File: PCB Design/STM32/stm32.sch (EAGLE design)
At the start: 58 parts, among them IC1 NCP1117ST50T3G, Q1 8MHz, T1 SFH303, T2 SFH303, T3 SFH303, T4 SFH303, U1 STM32F103RET6, U2 MCP1700T-3302E/TT, U3 MCP1700T-3302E/TT, U4 MPU-6050, U5 TB6612FNG

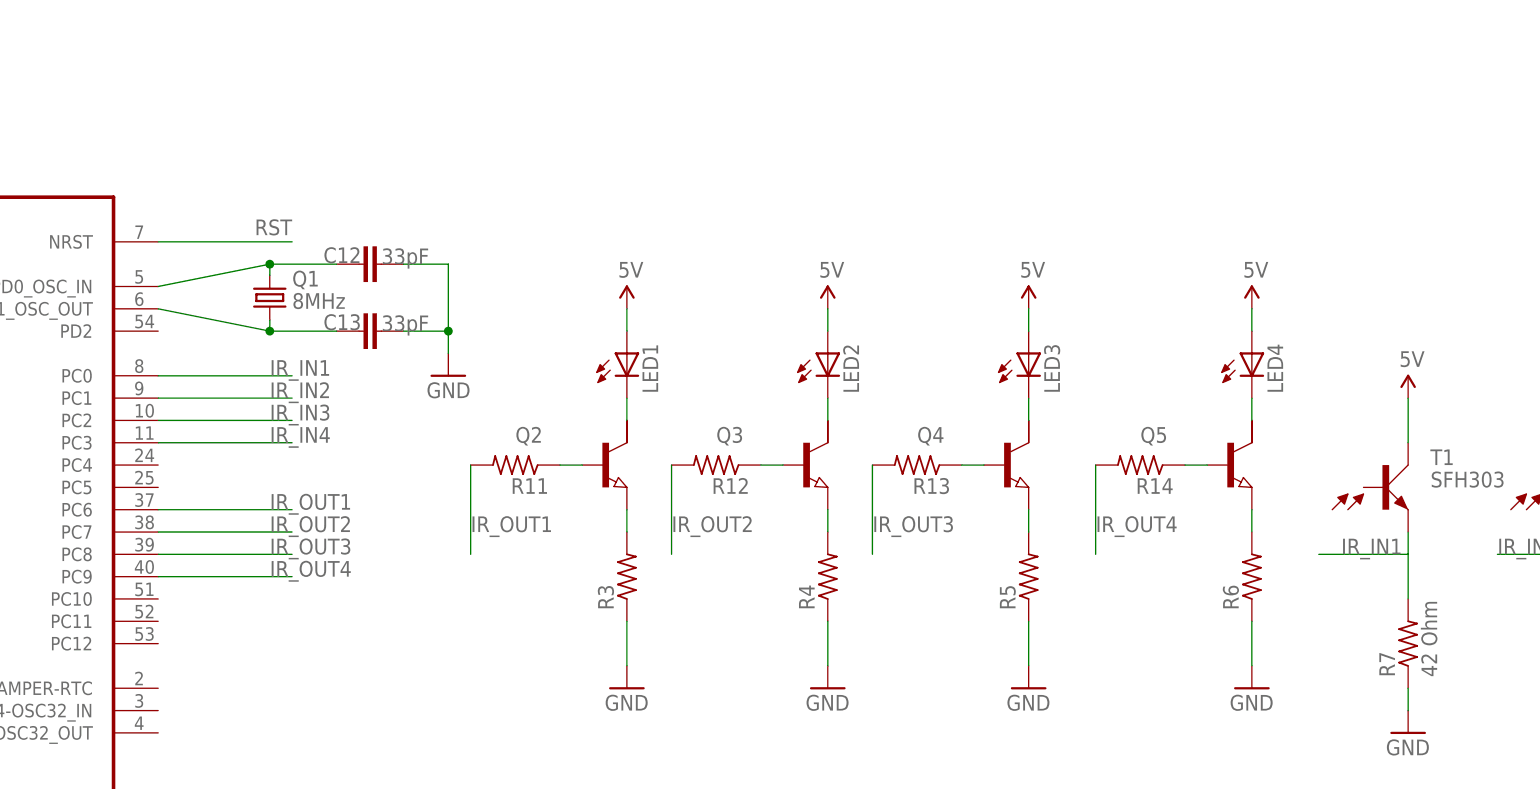
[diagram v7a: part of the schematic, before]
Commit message: added indicating leds
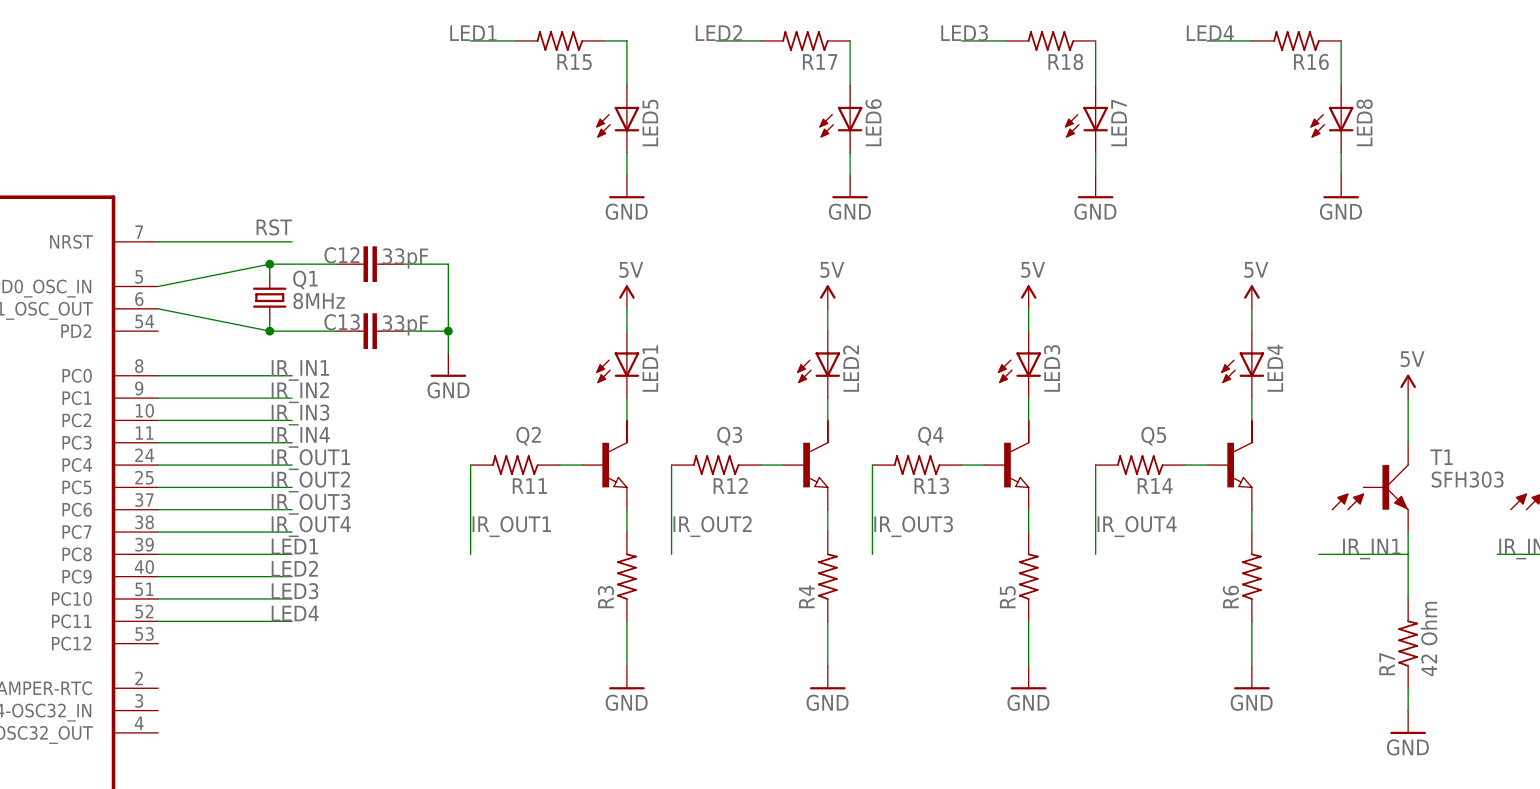
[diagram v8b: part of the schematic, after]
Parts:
- added LED5, LED6, LED7, LED8: (no value), eagle-ltspice:LED_ESML0603
- added R15, R16, R17, R18: (no value), resistor:R-US_R0603
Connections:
- new net LED1: R15.2, U1.PC8
- new net LED2: R17.2, U1.PC9
- new net LED3: R18.2
- new net LED4: R16.2
- new net N$26: LED5.A, R15.1
- new net N$27: LED6.A, R17.1
- new net N$28: LED7.A, R18.1
- new net N$29: LED8.A, R16.1
- net GND: now also LED5.C, LED6.C, LED7.C, LED8.C
- net IR_OUT1: no longer U1.PC6
- net IR_OUT2: no longer U1.PC7
- net IR_OUT3: now also U1.PC6; no longer U1.PC8
- net IR_OUT4: now also U1.PC7; no longer U1.PC9
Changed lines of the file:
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@@
 <?xml version="1.0" encoding="utf-8"?>
 <!DOCTYPE eagle SYSTEM "eagle.dtd">
-<eagle version="7.2.0">
+<eagle version="7.1.0">
 <drawing>
 <settings>
@@
 <part name="R13" library="resistor" deviceset="R-US_" device="R0603"/>
 <part name="R14" library="resistor" deviceset="R-US_" device="R0603"/>
+<part name="LED5" library="eagle-ltspice" deviceset="LED_E" device="SML0603"/>
+<part name="LED6" library="eagle-ltspice" deviceset="LED_E" device="SML0603"/>
+<part name="LED7" library="eagle-ltspice" deviceset="LED_E" device="SML0603"/>
+<part name="LED8" library="eagle-ltspice" deviceset="LED_E" device="SML0603"/>
+<part name="R15" library="resistor" deviceset="R-US_" device="R0603"/>
+<part name="R16" library="resistor" deviceset="R-US_" device="R0603"/>
+<part name="R17" library="resistor" deviceset="R-US_" device="R0603"/>
+<part name="R18" library="resistor" deviceset="R-US_" device="R0603"/>
+<part name="GND6" library="supply1" deviceset="GND" device=""/>
+<part name="GND29" library="supply1" deviceset="GND" device=""/>
+<part name="GND36" library="supply1" deviceset="GND" device=""/>
+<part name="GND37" library="supply1" deviceset="GND" device=""/>
 </parts>
 <sheets>
@@
 <instance part="R13" gate="G$1" x="309.88" y="236.22" rot="R180"/>
 <instance part="R14" gate="G$1" x="335.28" y="236.22" rot="R180"/>
+<instance part="LED5" gate="G$1" x="276.86" y="276.86"/>
+<instance part="LED6" gate="G$1" x="302.26" y="276.86"/>
+<instance part="LED7" gate="G$1" x="330.2" y="276.86"/>
+<instance part="LED8" gate="G$1" x="358.14" y="276.86"/>
+<instance part="R15" gate="G$1" x="269.24" y="284.48" rot="R180"/>
+<instance part="R16" gate="G$1" x="353.06" y="284.48" rot="R180"/>
+<instance part="R17" gate="G$1" x="297.18" y="284.48" rot="R180"/>
+<instance part="R18" gate="G$1" x="325.12" y="284.48" rot="R180"/>
+<instance part="GND6" gate="1" x="276.86" y="266.7"/>
+<instance part="GND29" gate="1" x="302.26" y="266.7"/>
+<instance part="GND36" gate="1" x="330.2" y="266.7"/>
+<instance part="GND37" gate="1" x="358.14" y="266.7"/>
 </instances>
 <busses>
@@
 <wire x1="347.98" y1="218.44" x2="347.98" y2="213.36" width="0.1524" layer="91"/>
 </segment>
+<segment>
+<pinref part="LED5" gate="G$1" pin="C"/>
+<pinref part="GND6" gate="1" pin="GND"/>
+<wire x1="276.86" y1="271.78" x2="276.86" y2="269.24" width="0.1524" layer="91"/>
+</segment>
+<segment>
+<pinref part="LED6" gate="G$1" pin="C"/>
+<pinref part="GND29" gate="1" pin="GND"/>
+<wire x1="302.26" y1="271.78" x2="302.26" y2="269.24" width="0.1524" layer="91"/>
+</segment>
+<segment>
+<pinref part="LED7" gate="G$1" pin="C"/>
+<pinref part="GND36" gate="1" pin="GND"/>
+<wire x1="330.2" y1="271.78" x2="330.2" y2="269.24" width="0.1524" layer="91"/>
+</segment>
+<segment>
+<pinref part="LED8" gate="G$1" pin="C"/>
+<pinref part="GND37" gate="1" pin="GND"/>
+<wire x1="358.14" y1="271.78" x2="358.14" y2="269.24" width="0.1524" layer="91"/>
+</segment>
 </net>
 <net name="VCC" class="0">
@@
 <net name="IR_OUT2" class="0">
 <segment>
-<wire x1="223.52" y1="228.6" x2="238.76" y2="228.6" width="0.1524" layer="91"/>
-<label x="236.22" y="228.6" size="1.778" layer="95"/>
-<pinref part="U1" gate="A" pin="PC7"/>
-</segment>
-<segment>
 <pinref part="R12" gate="G$1" pin="2"/>
 <wire x1="281.94" y1="236.22" x2="281.94" y2="226.06" width="0.1524" layer="91"/>
 <label x="281.94" y="228.6" size="1.778" layer="95"/>
 </segment>
+<segment>
+<wire x1="223.52" y1="233.68" x2="238.76" y2="233.68" width="0.1524" layer="91"/>
+<label x="236.22" y="233.68" size="1.778" layer="95"/>
+</segment>
 </net>
 <net name="IR_OUT1" class="0">
+<segment>
+<pinref part="R11" gate="G$1" pin="2"/>
+<wire x1="259.08" y1="236.22" x2="259.08" y2="226.06" width="0.1524" layer="91"/>
+<label x="259.08" y="228.6" size="1.778" layer="95"/>
+</segment>
+<segment>
+<wire x1="223.52" y1="236.22" x2="238.76" y2="236.22" width="0.1524" layer="91"/>
+<label x="236.22" y="236.22" size="1.778" layer="95"/>
+</segment>
+</net>
+<net name="IR_OUT3" class="0">
+<segment>
+<pinref part="R13" gate="G$1" pin="2"/>
+<wire x1="304.8" y1="236.22" x2="304.8" y2="226.06" width="0.1524" layer="91"/>
+<label x="304.8" y="228.6" size="1.778" layer="95"/>
+</segment>
 <segment>
 <wire x1="223.52" y1="231.14" x2="238.76" y2="231.14" width="0.1524" layer="91"/>
 <label x="236.22" y="231.14" size="1.778" layer="95"/>
 <pinref part="U1" gate="A" pin="PC6"/>
-</segment>
-<segment>
-<pinref part="R11" gate="G$1" pin="2"/>
-<wire x1="259.08" y1="236.22" x2="259.08" y2="226.06" width="0.1524" layer="91"/>
-<label x="259.08" y="228.6" size="1.778" layer="95"/>
-</segment>
-</net>
-<net name="IR_OUT3" class="0">
-<segment>
-<wire x1="223.52" y1="226.06" x2="238.76" y2="226.06" width="0.1524" layer="91"/>
-<label x="236.22" y="226.06" size="1.778" layer="95"/>
-<pinref part="U1" gate="A" pin="PC8"/>
-</segment>
-<segment>
-<pinref part="R13" gate="G$1" pin="2"/>
-<wire x1="304.8" y1="236.22" x2="304.8" y2="226.06" width="0.1524" layer="91"/>
-<label x="304.8" y="228.6" size="1.778" layer="95"/>
 </segment>
 </net>
@@
 <net name="IR_OUT4" class="0">
 <segment>
-<wire x1="223.52" y1="223.52" x2="238.76" y2="223.52" width="0.1524" layer="91"/>
-<label x="236.22" y="223.52" size="1.778" layer="95"/>
-<pinref part="U1" gate="A" pin="PC9"/>
-</segment>
-<segment>
 <pinref part="R14" gate="G$1" pin="2"/>
 <wire x1="330.2" y1="236.22" x2="330.2" y2="226.06" width="0.1524" layer="91"/>
 <label x="330.2" y="228.6" size="1.778" layer="95"/>
+</segment>
+<segment>
+<wire x1="223.52" y1="228.6" x2="238.76" y2="228.6" width="0.1524" layer="91"/>
+<label x="236.22" y="228.6" size="1.778" layer="95"/>
+<pinref part="U1" gate="A" pin="PC7"/>
 </segment>
 </net>
@@
 </segment>
 </net>
+<net name="N$26" class="0">
+<segment>
+<pinref part="R15" gate="G$1" pin="1"/>
+<pinref part="LED5" gate="G$1" pin="A"/>
+<wire x1="274.32" y1="284.48" x2="276.86" y2="284.48" width="0.1524" layer="91"/>
+<wire x1="276.86" y1="284.48" x2="276.86" y2="279.4" width="0.1524" layer="91"/>
+</segment>
+</net>
+<net name="N$27" class="0">
+<segment>
+<pinref part="R17" gate="G$1" pin="1"/>
+<pinref part="LED6" gate="G$1" pin="A"/>
+<wire x1="302.26" y1="284.48" x2="302.26" y2="279.4" width="0.1524" layer="91"/>
+</segment>
+</net>
+<net name="N$29" class="0">
+<segment>
+<pinref part="R16" gate="G$1" pin="1"/>
+<pinref part="LED8" gate="G$1" pin="A"/>
+<wire x1="358.14" y1="284.48" x2="358.14" y2="279.4" width="0.1524" layer="91"/>
+</segment>
+</net>
+<net name="N$28" class="0">
+<segment>
+<pinref part="R18" gate="G$1" pin="1"/>
+<pinref part="LED7" gate="G$1" pin="A"/>
+<wire x1="330.2" y1="284.48" x2="330.2" y2="279.4" width="0.1524" layer="91"/>
+</segment>
+</net>
+<net name="LED1" class="0">
+<segment>
+<wire x1="223.52" y1="226.06" x2="238.76" y2="226.06" width="0.1524" layer="91"/>
+<label x="236.22" y="226.06" size="1.778" layer="95"/>
+<pinref part="U1" gate="A" pin="PC8"/>
+</segment>
+<segment>
+<pinref part="R15" gate="G$1" pin="2"/>
+<wire x1="264.16" y1="284.48" x2="259.08" y2="284.48" width="0.1524" layer="91"/>
+<label x="256.54" y="284.48" size="1.778" layer="95"/>
+</segment>
+</net>
+<net name="LED2" class="0">
+<segment>
+<wire x1="223.52" y1="223.52" x2="238.76" y2="223.52" width="0.1524" layer="91"/>
+<label x="236.22" y="223.52" size="1.778" layer="95"/>
+<pinref part="U1" gate="A" pin="PC9"/>
+</segment>
+<segment>
+<pinref part="R17" gate="G$1" pin="2"/>
+<wire x1="292.1" y1="284.48" x2="287.02" y2="284.48" width="0.1524" layer="91"/>
+<label x="284.48" y="284.48" size="1.778" layer="95"/>
+</segment>
+</net>
+<net name="LED3" class="0">
+<segment>
+<wire x1="223.52" y1="220.98" x2="238.76" y2="220.98" width="0.1524" layer="91"/>
+<label x="236.22" y="220.98" size="1.778" layer="95"/>
+</segment>
+<segment>
+<pinref part="R18" gate="G$1" pin="2"/>
+<wire x1="320.04" y1="284.48" x2="314.96" y2="284.48" width="0.1524" layer="91"/>
+<label x="312.42" y="284.48" size="1.778" layer="95"/>
+</segment>
+</net>
+<net name="LED4" class="0">
+<segment>
+<wire x1="223.52" y1="218.44" x2="238.76" y2="218.44" width="0.1524" layer="91"/>
+<label x="236.22" y="218.44" size="1.778" layer="95"/>
+</segment>
+<segment>
+<pinref part="R16" gate="G$1" pin="2"/>
+<wire x1="347.98" y1="284.48" x2="342.9" y2="284.48" width="0.1524" layer="91"/>
+<label x="340.36" y="284.48" size="1.778" layer="95"/>
+</segment>
+</net>
